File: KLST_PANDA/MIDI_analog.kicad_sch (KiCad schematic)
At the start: 10 parts, among them J1 MIDI IN, J2 MIDI OUT, U1 H11L1SR2M, U2 74AHC1G125

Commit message: cleaned up main sheet
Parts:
- removed D1: 1N914WT, Diode_SMD:D_SOD-523, symbol Diode:1N914WT
- removed J1: MIDI IN, DIN-5:DIN5-RA-PTH, symbol Connector:DIN-5_180degree_with_Eaerth
- removed J2: MIDI OUT, DIN-5:DIN5-RA-PTH, symbol Connector:DIN-5_180degree_with_Eaerth
- added D13: 1N914WT, Diode_SMD:D_SOD-523, symbol Device:D_Small
- added J5 (x2): MIDI_IN, KLST_SHEEP:Korean_Hroparts_Elec_PJ-316A-6A, symbol Connector:AudioJack4_SwitchTR1
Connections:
- net GND: now also J5.R2, J5.S
- net MIDI_OUT_SINK(5): now reaches R4.1
- net MIDI_OUT_SINK(5): now also J5.T
- net MIDI_OUT_SOURCE(4): now reaches R1.2
- net MIDI_OUT_SOURCE(4): now also J5.R1
- net MIDI_IN_SOURCE(4): now reaches R3.1
- net MIDI_IN_SOURCE(4): now also J5.R1
- net at R3.2, U1.1: now also D13.1 (K)
- net MIDI_IN_SINK(5): now reaches U1.2
- net MIDI_IN_SINK(5): now also D13.2 (A), J5.T
- new net MIDI_IN_SHIELD(2): J5.R2, J5.S
- no-connect marks 9 -> 5
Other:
- note removed: "@TODO( replace DIN-5 connector with audio connector (TRS) with `Type A` allocation see https://minimidi.world )"
- note removed: "@TODO( the specs were wrong it s supposed to be 100nF(C49678) ( not 100uF(C696821) )."
- moved on the sheet: C1, R1, R3, R4, R6, U1, U2

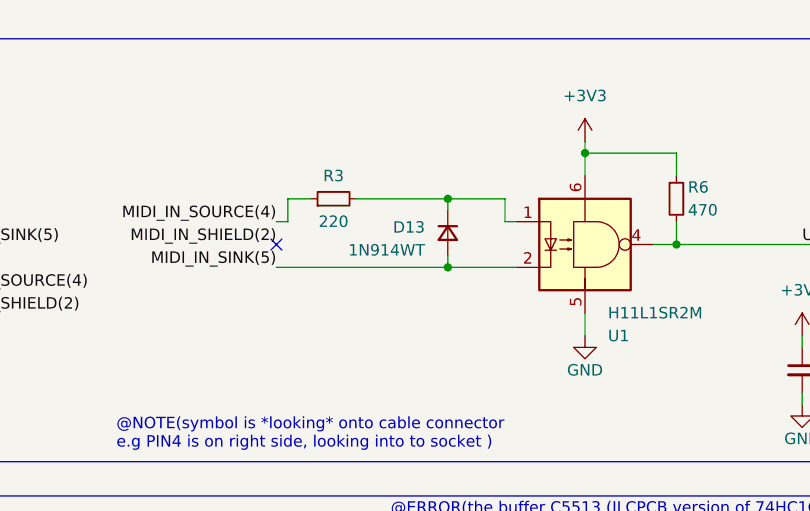
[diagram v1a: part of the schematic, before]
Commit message: improved GPIO, updated schematics
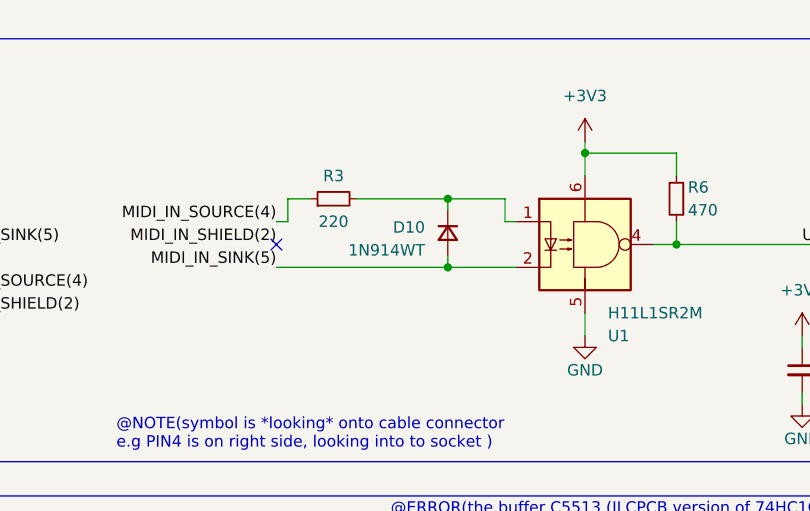
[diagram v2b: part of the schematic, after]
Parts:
- renumbered D13 to D10
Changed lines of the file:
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@@
         )
         (path "/b4513875-4c57-4720-bcc5-43ead67fe18f/1f0020ca-bef6-4e88-99dd-cc88d8a9362c"
-          (reference "J14") (unit 1)
+          (reference "J10") (unit 1)
         )
       )
@@
       (project "KLST_PANDA"
         (path "/b4513875-4c57-4720-bcc5-43ead67fe18f/1f0020ca-bef6-4e88-99dd-cc88d8a9362c"
-          (reference "R69") (unit 1)
+          (reference "R65") (unit 1)
         )
       )
@@
       (project "KLST_PANDA"
         (path "/b4513875-4c57-4720-bcc5-43ead67fe18f/1f0020ca-bef6-4e88-99dd-cc88d8a9362c"
-          (reference "#PWR047") (unit 1)
+          (reference "#PWR079") (unit 1)
         )
       )
@@
       (project "KLST_PANDA"
         (path "/b4513875-4c57-4720-bcc5-43ead67fe18f/1f0020ca-bef6-4e88-99dd-cc88d8a9362c"
-          (reference "C61") (unit 1)
+          (reference "C70") (unit 1)
         )
       )
@@
       (project "KLST_PANDA"
         (path "/b4513875-4c57-4720-bcc5-43ead67fe18f/1f0020ca-bef6-4e88-99dd-cc88d8a9362c"
-          (reference "#PWR051") (unit 1)
+          (reference "#PWR081") (unit 1)
         )
       )
@@
       (project "KLST_PANDA"
         (path "/b4513875-4c57-4720-bcc5-43ead67fe18f/1f0020ca-bef6-4e88-99dd-cc88d8a9362c"
-          (reference "R66") (unit 1)
+          (reference "R64") (unit 1)
         )
       )
@@
       (project "KLST_PANDA"
         (path "/b4513875-4c57-4720-bcc5-43ead67fe18f/1f0020ca-bef6-4e88-99dd-cc88d8a9362c"
-          (reference "R68") (unit 1)
+          (reference "R63") (unit 1)
         )
       )
@@
       (project "KLST_PANDA"
         (path "/b4513875-4c57-4720-bcc5-43ead67fe18f/1f0020ca-bef6-4e88-99dd-cc88d8a9362c"
-          (reference "U3") (unit 1)
+          (reference "U5") (unit 1)
         )
       )
@@
       (project "KLST_PANDA"
         (path "/b4513875-4c57-4720-bcc5-43ead67fe18f/1f0020ca-bef6-4e88-99dd-cc88d8a9362c"
-          (reference "#PWR045") (unit 1)
+          (reference "#PWR076") (unit 1)
         )
       )
@@
       (project "KLST_PANDA"
         (path "/b4513875-4c57-4720-bcc5-43ead67fe18f/1f0020ca-bef6-4e88-99dd-cc88d8a9362c"
-          (reference "#PWR043") (unit 1)
+          (reference "#PWR074") (unit 1)
         )
       )
@@
       (project "KLST_PANDA"
         (path "/b4513875-4c57-4720-bcc5-43ead67fe18f/1f0020ca-bef6-4e88-99dd-cc88d8a9362c"
-          (reference "#PWR052") (unit 1)
+          (reference "#PWR082") (unit 1)
         )
       )
@@
       (project "KLST_PANDA"
         (path "/b4513875-4c57-4720-bcc5-43ead67fe18f/1f0020ca-bef6-4e88-99dd-cc88d8a9362c"
-          (reference "#PWR049") (unit 1)
+          (reference "#PWR078") (unit 1)
         )
       )
@@
       (project "KLST_PANDA"
         (path "/b4513875-4c57-4720-bcc5-43ead67fe18f/1f0020ca-bef6-4e88-99dd-cc88d8a9362c"
-          (reference "#PWR048") (unit 1)
+          (reference "#PWR080") (unit 1)
         )
       )
@@
       (project "KLST_PANDA"
         (path "/b4513875-4c57-4720-bcc5-43ead67fe18f/1f0020ca-bef6-4e88-99dd-cc88d8a9362c"
-          (reference "#PWR046") (unit 1)
+          (reference "#PWR077") (unit 1)
         )
       )
@@
       (project "KLST_PANDA"
         (path "/b4513875-4c57-4720-bcc5-43ead67fe18f/1f0020ca-bef6-4e88-99dd-cc88d8a9362c"
-          (reference "R71") (unit 1)
+          (reference "R66") (unit 1)
         )
       )
@@
       (project "KLST_PANDA"
         (path "/b4513875-4c57-4720-bcc5-43ead67fe18f/1f0020ca-bef6-4e88-99dd-cc88d8a9362c"
-          (reference "#PWR041") (unit 1)
+          (reference "#PWR075") (unit 1)
         )
       )
@@
         )
         (path "/b4513875-4c57-4720-bcc5-43ead67fe18f/1f0020ca-bef6-4e88-99dd-cc88d8a9362c"
-          (reference "J15") (unit 1)
+          (reference "J11") (unit 1)
         )
       )
@@
   (symbol (lib_id "Device:D_Small") (at 152.4 60.96 270) (unit 1)
     (in_bom yes) (on_board yes) (dnp no)
-    (property "Reference" "D13" (at 149.86 60.325 90)
+    (property "Reference" "D10" (at 149.86 60.325 90)
       (effects (font (size 1.27 1.27)) (justify right))
     )
@@
       (project "KLST_PANDA"
         (path "/b4513875-4c57-4720-bcc5-43ead67fe18f/1f0020ca-bef6-4e88-99dd-cc88d8a9362c"
-          (reference "D13") (unit 1)
+          (reference "D10") (unit 1)
         )
       )
@@
       (project "KLST_PANDA"
         (path "/b4513875-4c57-4720-bcc5-43ead67fe18f/1f0020ca-bef6-4e88-99dd-cc88d8a9362c"
-          (reference "U5") (unit 1)
-        )
-      )
+          (reference "U6") (unit 1)
+        )
+      )

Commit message: added mechanical keys, updated audio jacks, minor changes
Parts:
- J5: footprint KLST_SHEEP:Korean_Hroparts_Elec_PJ-316A-6A -> PJ-316A-6A:PJ-316A-6A
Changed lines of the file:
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@@
       (effects (font (size 1.27 1.27)) (justify right))
     )
-    (property "Footprint" "KLST_SHEEP:Korean_Hroparts_Elec_PJ-316A-6A" (at 86.36 67.31 0)
+    (property "Footprint" "PJ-316A-6A:PJ-316A-6A" (at 86.36 67.31 0)
       (effects (font (size 1.27 1.27)) hide)
     )
@@
       (effects (font (size 1.27 1.27)) (justify right))
     )
-    (property "Footprint" "KLST_SHEEP:Korean_Hroparts_Elec_PJ-316A-6A" (at 86.36 118.11 0)
-      (effects (font (size 1.27 1.27)) hide)
-    )
+    (property "Footprint" "PJ-316A-6A:PJ-316A-6A" (at 86.36 118.11 0)
+      (effects (font (size 1.27 1.27)) hide)
+    )

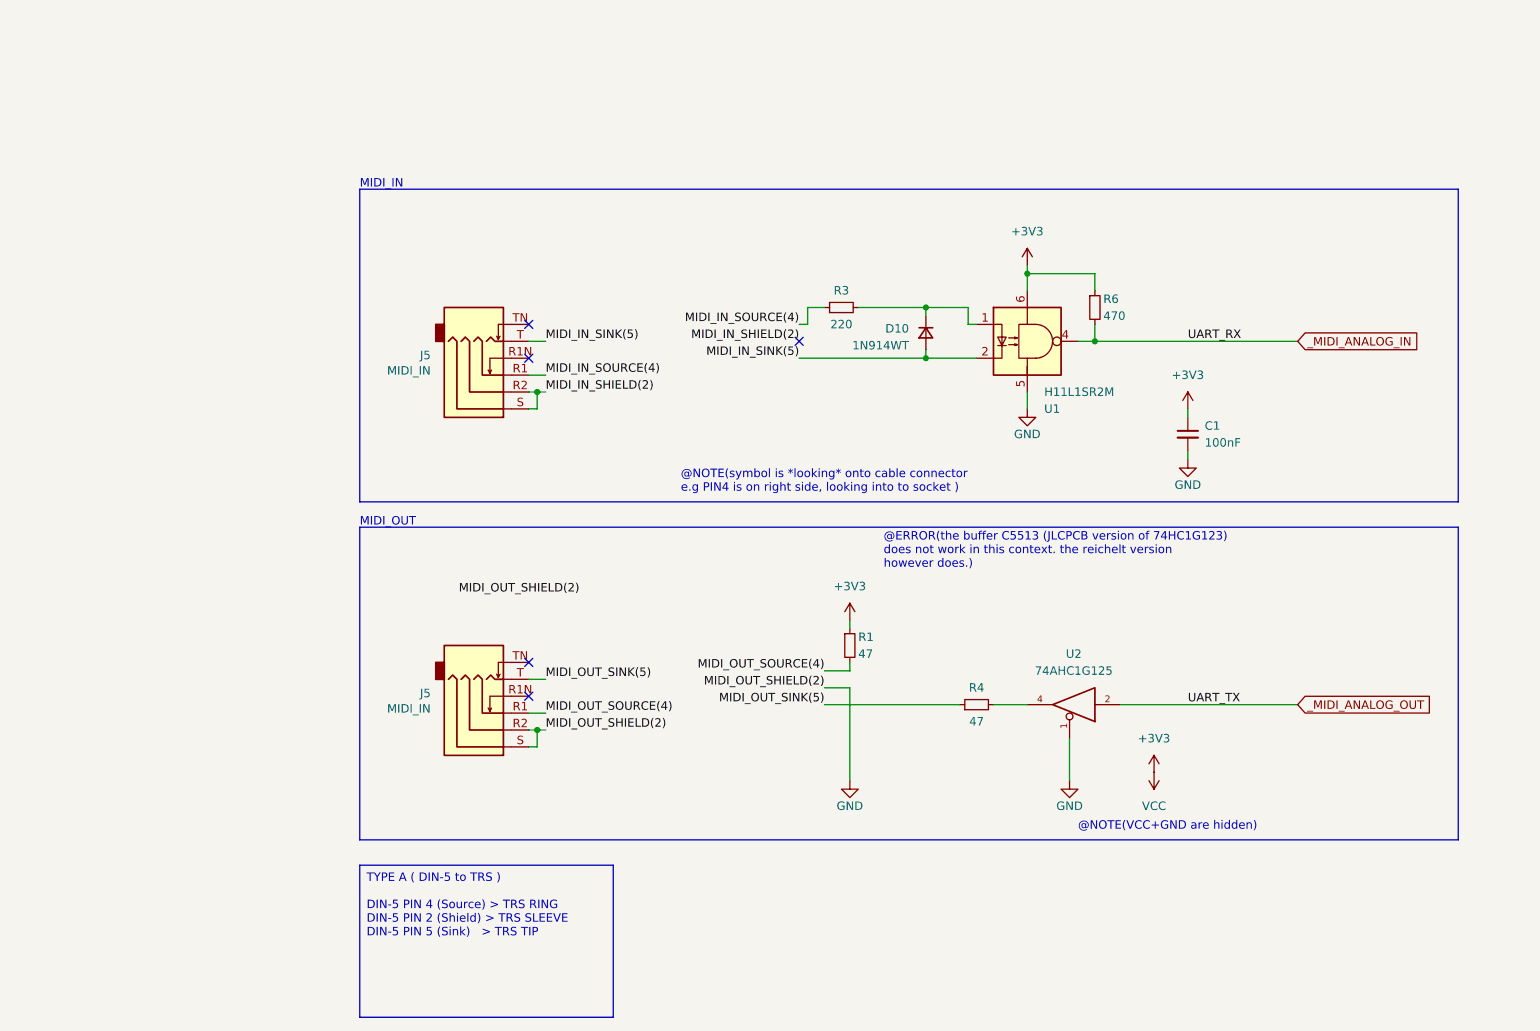
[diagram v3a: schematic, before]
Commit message: moved core (MCU) to sheet, cleaned up sheets
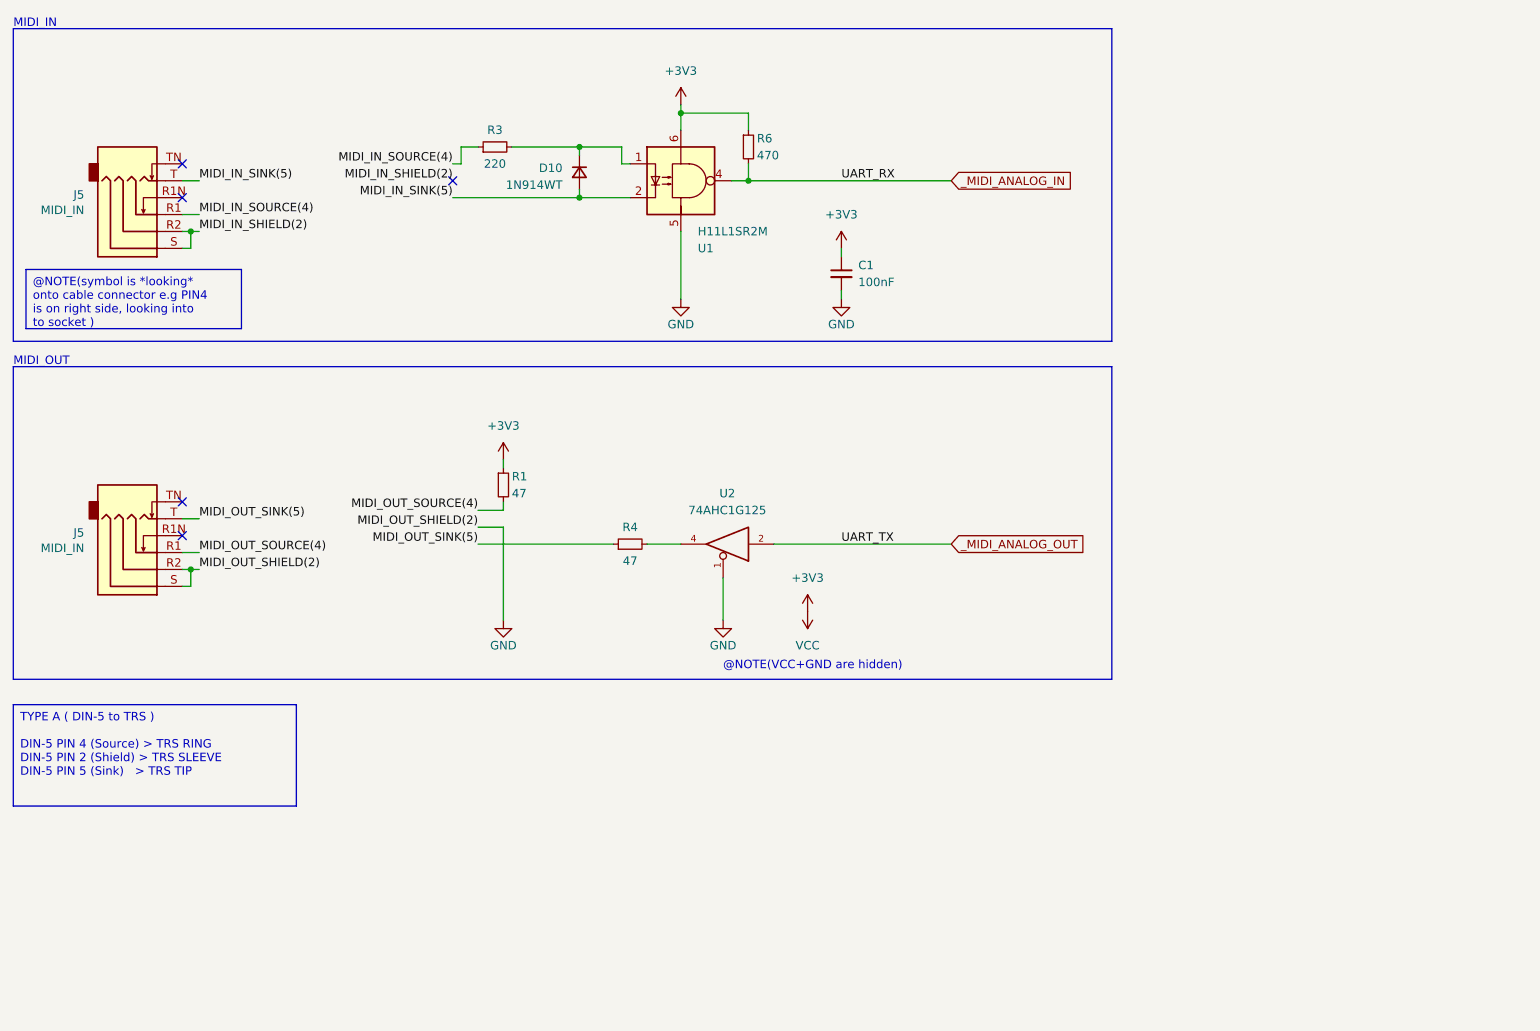
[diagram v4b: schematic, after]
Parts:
- U2: footprint Package_TO_SOT_SMD:SOT-23-5_HandSoldering -> Package_TO_SOT_SMD:SOT-353_SC-70-5; LCSC C5513 -> C151890
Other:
- note removed: "@ERROR(the buffer C5513 (JLCPCB version of 74HC1G123) does not work in this context. the reichelt version however does.)"
- note removed: "@NOTE(symbol is *looking* onto cable connector e.g PIN4 is on right side, looking into to socket )"
- moved on the sheet: C1, D10, J5, R1, R3, R4, R6, U1, U2

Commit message: started cleaning up schematic ( addressing DRC errors/warning ) (WIP)
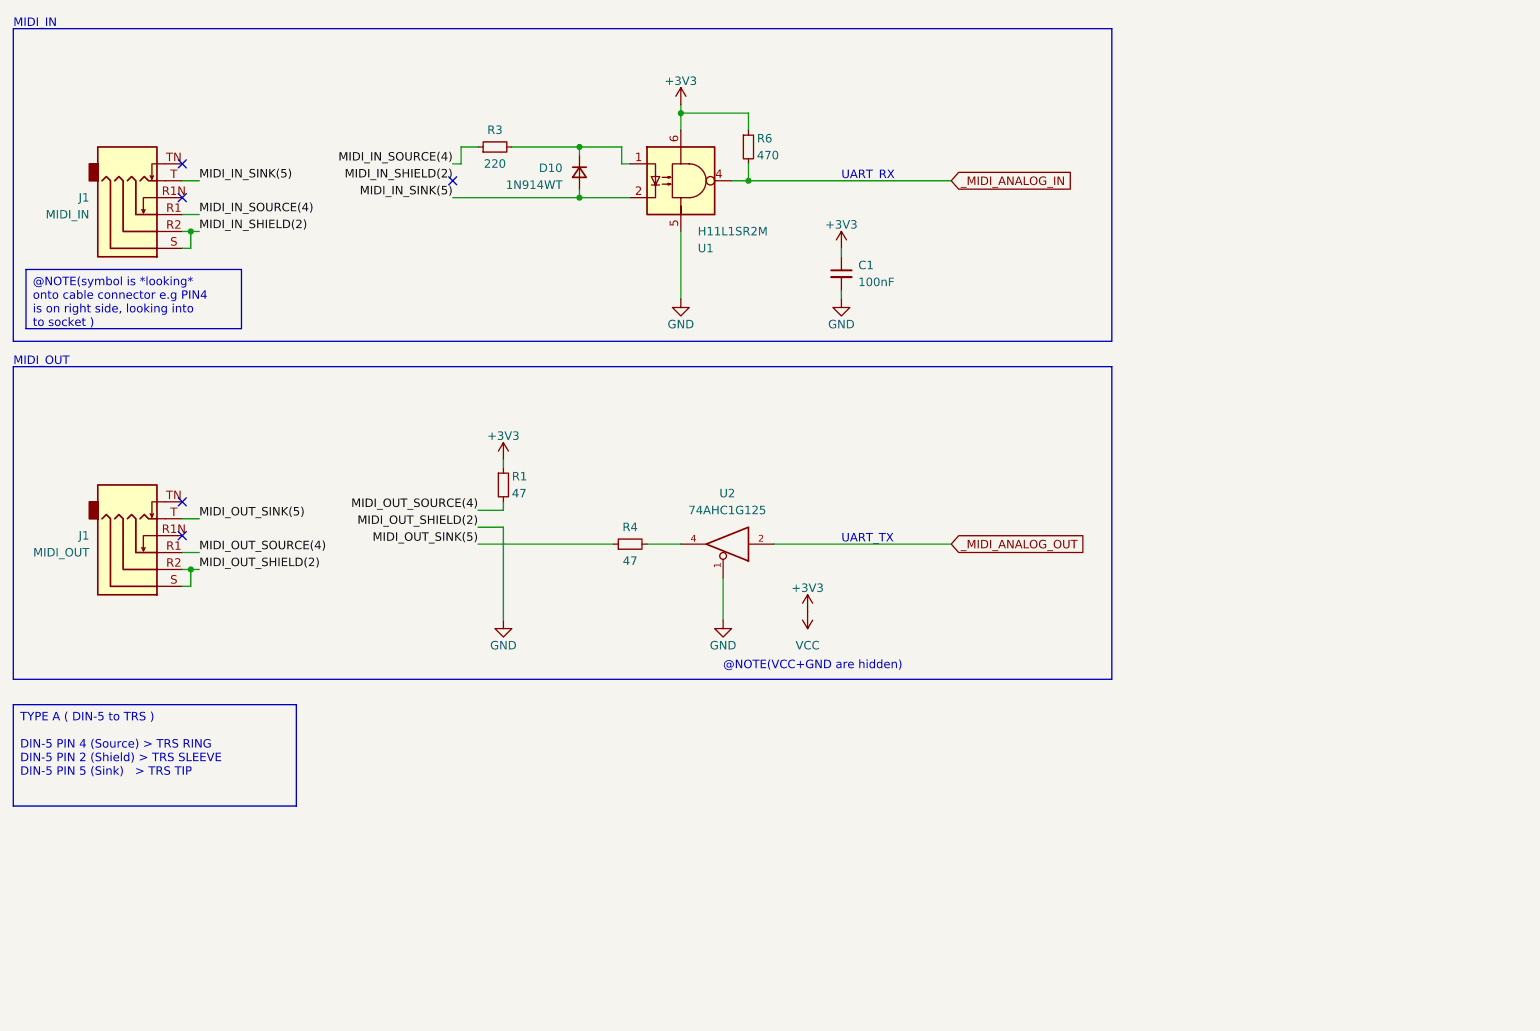
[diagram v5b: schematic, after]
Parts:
- removed J5 (x2): MIDI_IN, PJ-316A-6A:PJ-316A-6A, symbol Connector:AudioJack4_SwitchTR1
- added J1: MIDI_OUT, symbol Connector_Audio:AudioJack4_SwitchTR1
- added J1: MIDI_IN, symbol Connector_Audio:AudioJack4_SwitchTR1
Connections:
- net GND: now also J1.R2, J1.S
- net MIDI_IN_SHIELD(2): now also J1.R2, J1.S
- net MIDI_IN_SINK(5): now also J1.T
- net MIDI_IN_SOURCE(4): now also J1.R1
- net MIDI_OUT_SINK(5): now also J1.T
- net MIDI_OUT_SOURCE(4): now also J1.R1
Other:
- note added: "UART_RX"
- note added: "UART_TX"

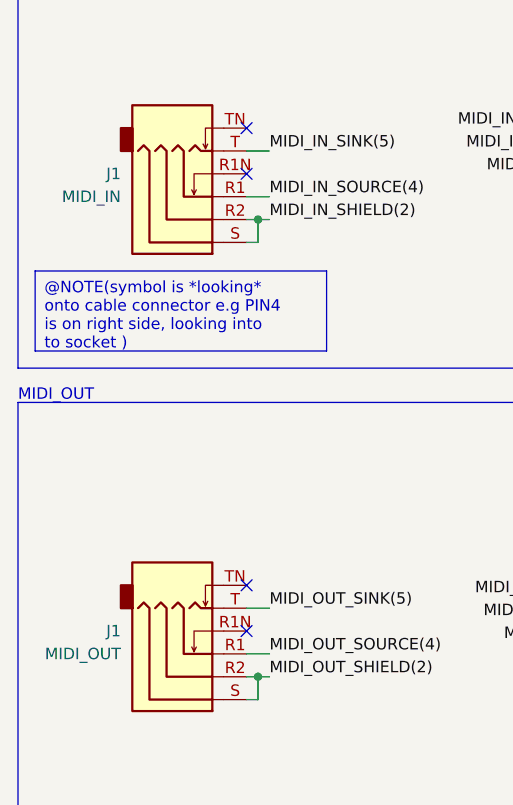
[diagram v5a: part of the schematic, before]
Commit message: added battery clip, updated to new KiCad version
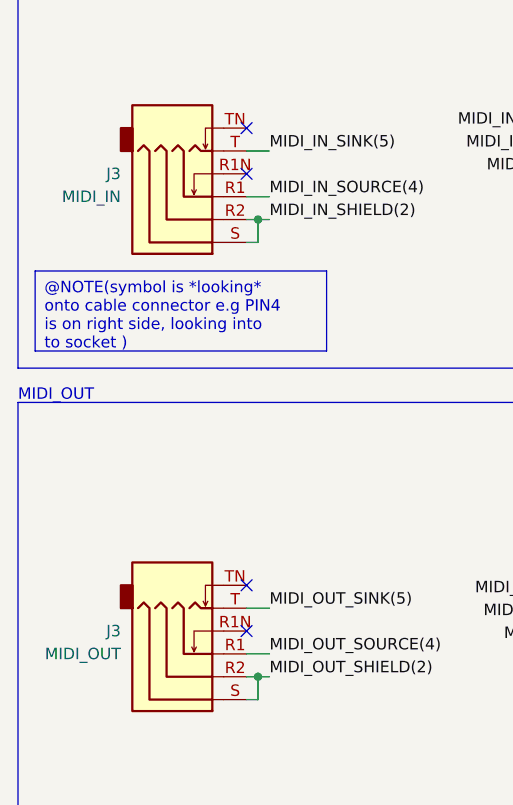
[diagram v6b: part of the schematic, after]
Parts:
- removed J1: MIDI_OUT, symbol Connector_Audio:AudioJack4_SwitchTR1
- removed J1: MIDI_IN, symbol Connector_Audio:AudioJack4_SwitchTR1
- added J3: MIDI_OUT, PJ-316A-6A:PJ-316A-6A, symbol Connector_Audio:AudioJack4_SwitchTR1
- added J3: MIDI_IN, PJ-316A-6A:PJ-316A-6A, symbol Connector_Audio:AudioJack4_SwitchTR1
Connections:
- net GND: now also J3.R2, J3.S
- net MIDI_IN_SHIELD(2): now also J3.R2, J3.S
- net MIDI_IN_SINK(5): now also J3.T
- net MIDI_IN_SOURCE(4): now also J3.R1
- net MIDI_OUT_SINK(5): now also J3.T
- net MIDI_OUT_SOURCE(4): now also J3.R1

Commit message: updated 74AHC1G125 symbol
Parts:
- removed U2: 74AHC1G125, Package_TO_SOT_SMD:SOT-353_SC-70-5, symbol 74xGxx:74AHC1G125
- added U10: 74AHC1G125, symbol 74xGxx:74AHC1G125
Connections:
- net +3V3: now also U10.5 (VCC)
- net GND: now also U10.1, U10.3 (GND)
- net _MIDI_ANALOG_OUT: now also U10.2
- net at R4.2: now also U10.4
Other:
- note removed: "@NOTE(VCC+GND are hidden)"
- moved on the sheet: C1, R4
